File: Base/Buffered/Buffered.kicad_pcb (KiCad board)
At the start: 2 copper layers, 30 x 84 mm, 19 parts, among them J1 Conn_01x04_Pin, J2 Conn_01x04_Pin, J3 AudioJack2_Ground, J4 AudioJack2_Ground, J5 Barrel_Jack_Switch, Q1 40V, Q2 DMC3071LVT

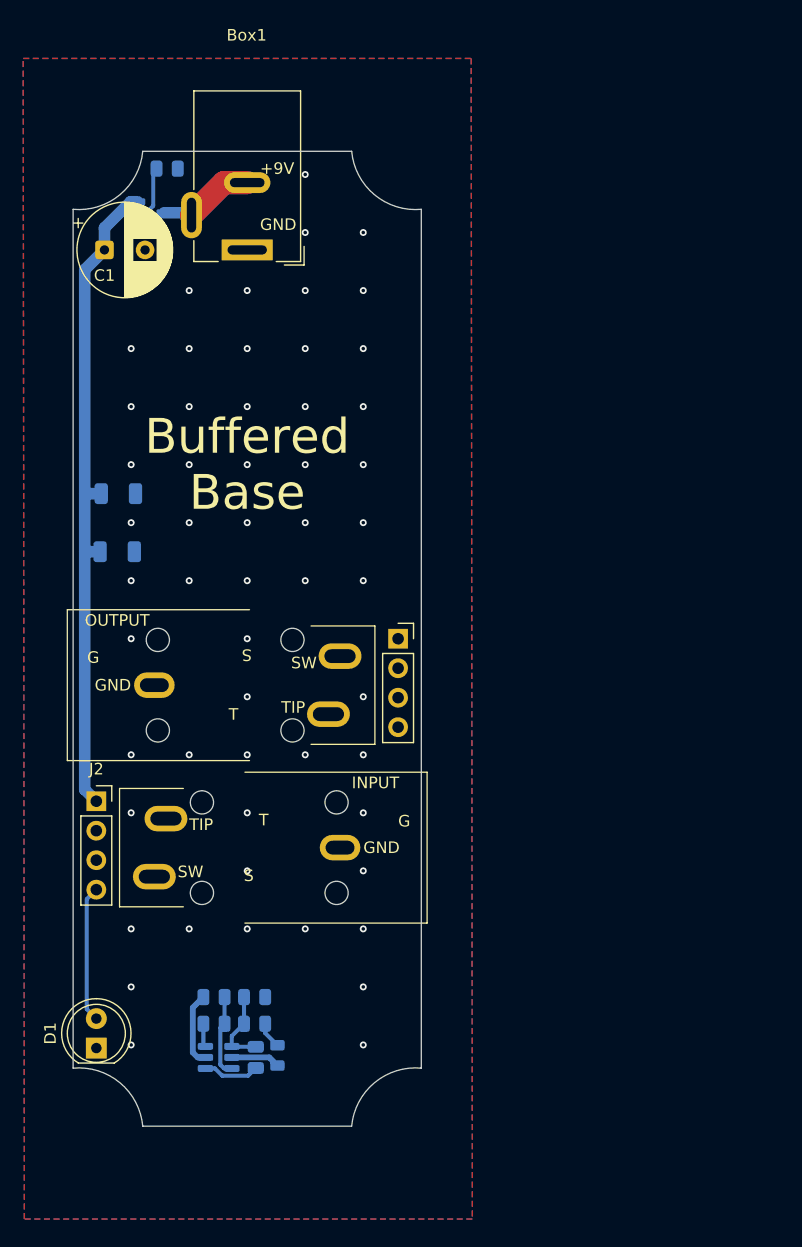
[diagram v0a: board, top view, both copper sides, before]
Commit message: Wire the soft-switch up to actually switch signal and LED
Surprisingly, this actually seems to work fine.  In simulation only, of
course.

And not surprisingly, according to the same simulation, it has an
impressively horrible pop at switching time.  This very much reminds me
of the broken "Tremolo doubling as a metronome" thing, which was due to
the exact same thing: very harsh and sudden driving of the JFET gate.

It's made worse by the MOSFET switching having the same thing.  Big
voltage spike when turning off, presumably due to capacitive parasitics
or whatever.

Possibly helped by adding a resistor at the gate or something, but
unlike the tremolo, the switching event is rare.  So right now I simply
don't care.  I'm just _simulating_ switching things at a 5Hz rate, so it
shows up like a sore thumb.

I haven't done layout, and I haven't added a real switch yet, so this is
all just simulation.

Signed-off-by: Linus Torvalds <torvalds@linux-foundation.org>
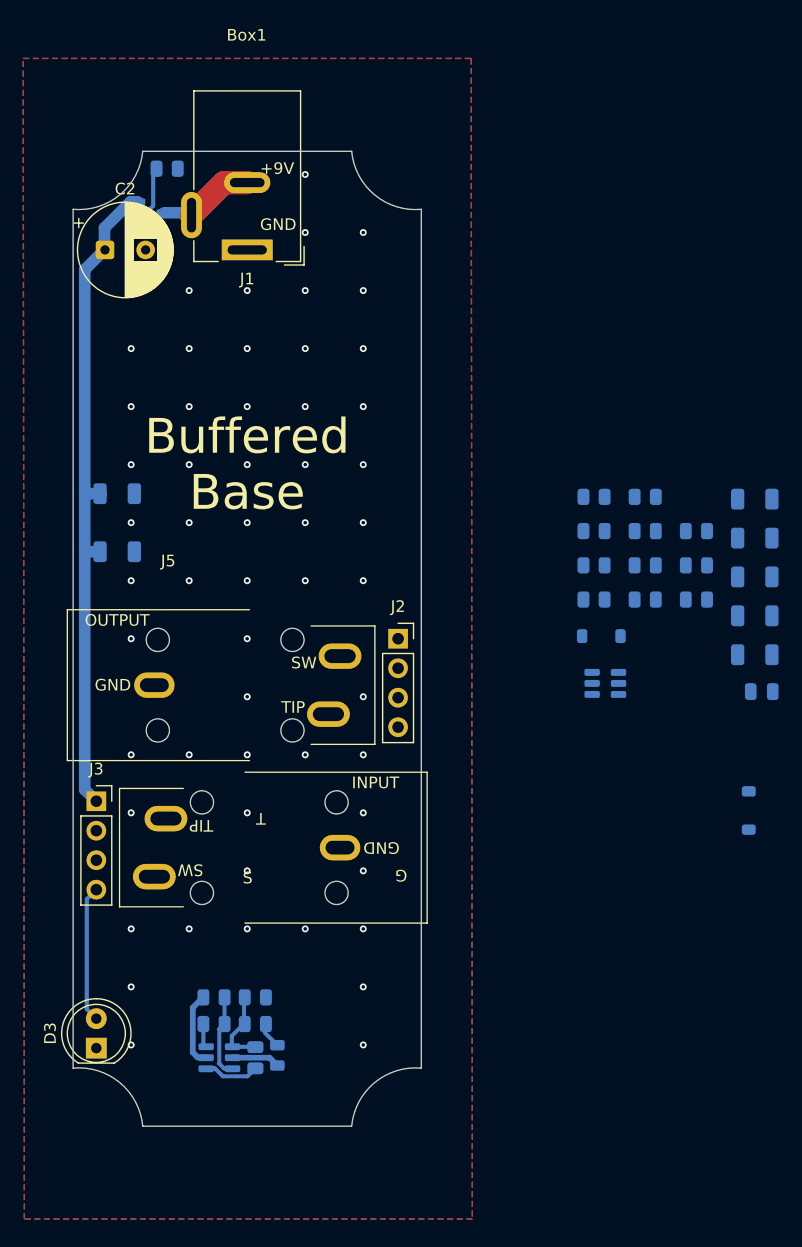
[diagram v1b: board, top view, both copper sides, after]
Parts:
- removed R1: 100k, Resistor_SMD:R_0805_2012Metric
- added C10: 1uF, Capacitor_SMD:C_1206_3216Metric, B.Cu at (143.7, 101.4)
- added C5: 1uF, Capacitor_SMD:C_1206_3216Metric, B.Cu at (143.7, 88.0)
- added C6: 1uF, Capacitor_SMD:C_1206_3216Metric, B.Cu at (143.7, 91.3)
- added C7: 0.47uF, Capacitor_SMD:C_1206_3216Metric, B.Cu at (143.7, 94.7)
- added C8: 220pF, Capacitor_SMD:C_0805_2012Metric, B.Cu at (144.3, 104.6)
- added C9: 1uF, Capacitor_SMD:C_1206_3216Metric, B.Cu at (143.7, 98.0)
- added D2: BAT41Z, Diode_SMD:D_SOD-123, B.Cu at (130.5, 99.8)
- added D3: LED, LED_THT:LED_D5.0mm, F.Cu at (87.0, 135.3)
- added Q3: LS844, Package_TO_SOT_SMD:SOT-23-6, B.Cu at (130.9, 103.8)
- added R10: 1MEG, Resistor_SMD:R_0805_2012Metric, B.Cu at (138.7, 96.6)
- added R11: 1MEG, Resistor_SMD:R_0805_2012Metric, B.Cu at (134.3, 87.8)
- added R12: 1k, Resistor_SMD:R_0805_2012Metric, B.Cu at (134.3, 90.7)
- added R13: 1MEG, Resistor_SMD:R_0805_2012Metric, B.Cu at (134.3, 93.7)
- added R14: 22k, Resistor_SMD:R_0805_2012Metric, B.Cu at (134.3, 96.6)
- added R15: 22k, Resistor_SMD:R_0805_2012Metric, B.Cu at (129.9, 87.8)
- added R16: 22k, Resistor_SMD:R_0805_2012Metric, B.Cu at (129.9, 90.7)
- added R17: 22k, Resistor_SMD:R_0805_2012Metric, B.Cu at (129.9, 93.7)
- added R18: 2k2, Resistor_SMD:R_0805_2012Metric, B.Cu at (129.9, 96.6)
- added R7: 22k, Resistor_SMD:R_0805_2012Metric, B.Cu at (100.7, 130.9)
- added R8: 1MEG, Resistor_SMD:R_0805_2012Metric, B.Cu at (138.7, 90.7)
- added R9: 1MEG, Resistor_SMD:R_0805_2012Metric, B.Cu at (138.7, 93.7)
- C1: value 100uF -> 0.1uF; footprint Capacitor_THT:CP_Radial_D8.0mm_P3.50mm -> Mylib:C_0704_1810Metric; moved to B.Cu
- C2: value 10uF -> 100uF; footprint Capacitor_SMD:C_1206_3216Metric -> Capacitor_THT:CP_Radial_D8.0mm_P3.50mm; moved to F.Cu
- C3: value 1uF -> 10uF
- C4: value 0.1uF -> 1uF; footprint Mylib:C_0704_1810Metric -> Capacitor_SMD:C_1206_3216Metric
- D1: value LED -> BAT41Z; footprint LED_THT:LED_D5.0mm -> Diode_SMD:D_SOD-123; moved to B.Cu
- J1: value Conn_01x04_Pin -> Barrel_Jack_Switch; footprint Connector_PinSocket_2.54mm:PinSocket_1x04_P2.54mm_Vertical -> Connector_BarrelJack:BarrelJack_Wuerth_6941xx301002
- J3: value AudioJack2_Ground -> Conn_01x04_Pin; footprint Mylib:CK-6.35 -> Connector_PinSocket_2.54mm:PinSocket_1x04_P2.54mm_Vertical
- J5: value Barrel_Jack_Switch -> AudioJack2_Ground; footprint Connector_BarrelJack:BarrelJack_Wuerth_6941xx301002 -> Mylib:CK-6.35
- Q1: value 40V -> DMC3071LVT; footprint Package_TO_SOT_SMD:SOT-23-3 -> Package_TO_SOT_SMD:TSOT-23-6
- Q2: value DMC3071LVT -> 40V; footprint Package_TO_SOT_SMD:TSOT-23-6 -> Package_TO_SOT_SMD:SOT-23-3
- R4: value 22k -> 100k
- R5: value 220k -> 22k
- R6: value 22k -> 220k
- moved Q1 73.0 mm to (97.6, 136.1)
- moved Q2 73.0 mm to (91.7, 63.3)
- moved R4 71.8 mm to (93.1, 59.5), turned to 0 degrees
- moved C1 71.0 mm to (102.6, 135.9), turned to -90 degrees
- moved D1 59.8 mm to (143.2, 114.8)
- moved C4 50.3 mm to (88.8, 87.5), turned to 0 degrees
- moved J5 38.3 mm to (92.0, 104.0), turned to 0 degrees
- moved J1 35.9 mm to (100.0, 66.5), turned to 180 degrees
- moved J2 29.5 mm to (113.0, 100.0)
- moved J3 21.4 mm to (87.0, 114.0), turned to 0 degrees
- moved J4 21.3 mm to (108.0, 118.0), turned to 180 degrees
- moved C2 21.0 mm to (87.7, 66.5)
- moved R5 2.93 mm to (100.7, 136.1), turned to -90 degrees
- moved R6 2.88 mm to (100.7, 133.2), turned to 180 degrees
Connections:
- C1 pad 1: VIN -> SW2
- C4 pad 1: SW2 -> VIN
- D1 pad 1: GND -> Net-(D1-K)
- D1 pad 2: LED -> GATE^{OFF}
- J1 pad 1: IN^{EFF} -> GND
- J1 pad 2: GND -> PWRIN
- J1 pad 3: GND -> PWRIN
- J2 pad 1: VIN -> IN^{EFF}
- J2 pad 4: LED -> OUT^{EFF}
- J4 pad S: unconnected-(J4-PadS) -> GND
- J4 pad T: OUT^{CONN} -> IN^{CONN}
- Q1 pad 1: Net-(Q1-G) -> Net-(Q1A-G)
- Q1 pad 3: PWRIN -> SW1
- Q2 pad 1: Net-(Q2A-G) -> Net-(Q2-G)
- Q2 pad 3: SW1 -> PWRIN
- R4 pad 1: GND -> Net-(Q2-G)
- R4 pad 2: ON_HIGH -> GND
- R5 pad 1: SW2 -> ON_HIGH
- R5 pad 2: ON_HIGH -> Net-(Q1A-G)
- R6 pad 1: ON_HIGH -> SW2
- R6 pad 2: Net-(Q2A-G) -> ON_HIGH
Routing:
- net Net-(Q2-G): track 0.00 -> 5.42 mm
- net Net-(Q1-G): track 5.42 -> 0.00 mm
- net Net-(Q1A-G): track 0.00 -> 4.91 mm
- net Net-(Q2A-G): track 4.87 -> 0.00 mm

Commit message: Split the buffered base over multiple schematic pages, do PCB layout
So this thing is still mis-named, in that it doesn't actually buffer the
signal at all, it only does the transistor soft-switching.  But I _will_
add buffering at some point, it's just not the interesting part of this
all, since I've done that part before.

But because I wrote explanations for the push-on / push-off circuit, and
because I split things up into small parts, the schematic was getting
pretty crowded.  So I decided to split up the actually interesting part
of the schematic - the switching side - onto a schematic page of its
own.

And while doing that, I moved the simulation infrastructure to its own
page too.

That leaves the toplevel page pretty empty with mainly just the
connectors and the basic signal and power filtering, but that's where
the buffers will go eventually.

And because it simulates fine, I want to actually see if it works in
reality.  So this also does the PCB layout.  There's tons of room left
for any future buffering circuit, whether I then do it with discrete
JFETs or decide that op-amps are the sane thing here.

I used a random regular tactile switch - which I don't actually have in
my parts library.  I'll just wire up two wires and test it that way (and
I do have some momentary SPDT stomp switches around that I can attach to
the wires).

But longer-term, one of the points of this kind of electronic switching
is that you can do it multiple ways, and aren't limited to a physical
switch - or indeed just a single one.  So maybe I'll do some remote
switching thing, or play around with using a hall effect sensor and a
magnet, or whatever.

There are always new things to learn about...  But let's make sure the
basics of this thing actually works first.

Signed-off-by: Linus Torvalds <torvalds@linux-foundation.org>
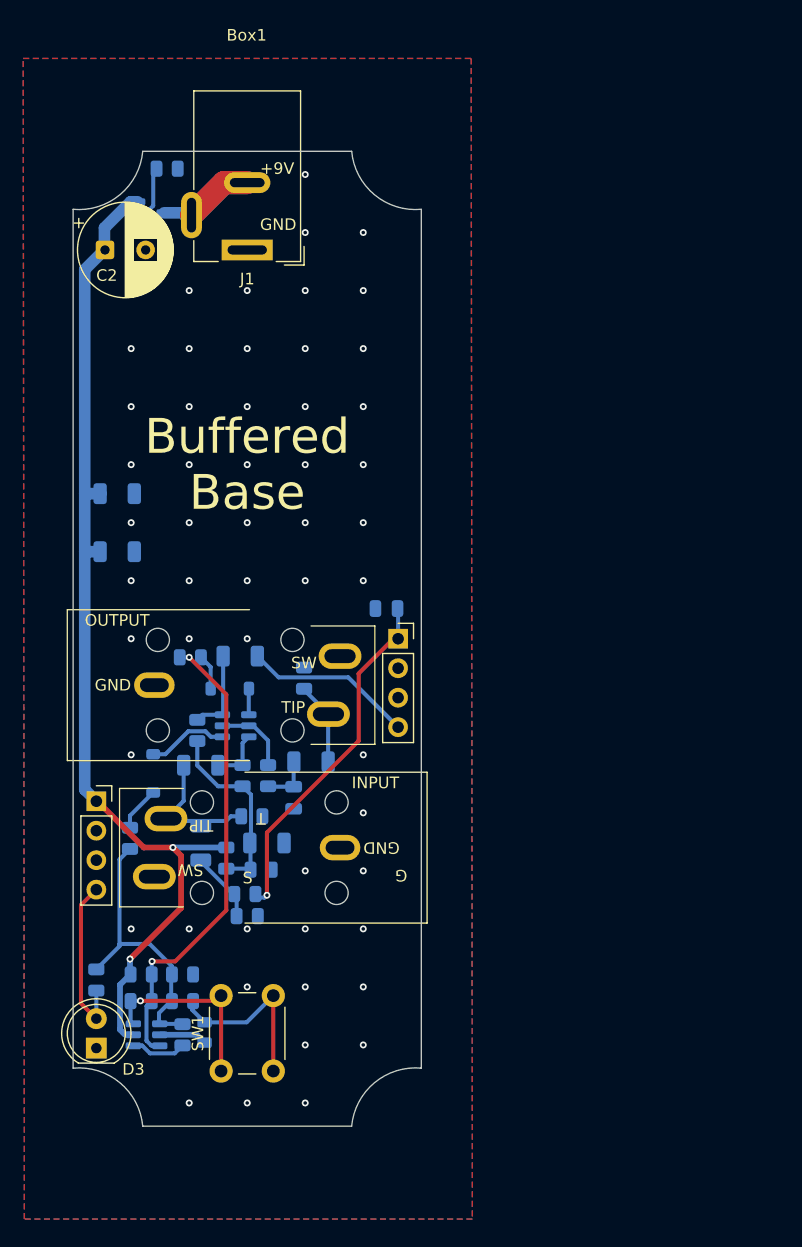
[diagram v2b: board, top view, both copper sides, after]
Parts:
- added C11: 150pF, Capacitor_SMD:C_0805_2012Metric, B.Cu at (104.0, 113.7)
- added R23: 1k, Resistor_SMD:R_0805_2012Metric, B.Cu at (101.8, 111.8)
- added SW1: SW_Push, Button_Switch_THT:SW_PUSH_6mm, F.Cu at (97.8, 137.2)
- C8: value 220pF -> 150pF
- R15: value 22k -> 47k
- moved R18 54.0 mm to (87.0, 129.4), turned to 90 degrees
- moved C7 53.0 mm to (96.0, 117.6), turned to -90 degrees
- moved C6 51.6 mm to (96.0, 110.9), turned to 0 degrees
- moved R11 49.8 mm to (100.0, 123.9), turned to 0 degrees
- moved R12 46.6 mm to (99.8, 122.0), turned to 0 degrees
- moved R17 46.4 mm to (89.9, 117.2), turned to -90 degrees
- moved C5 46.4 mm to (99.4, 101.5)
- moved R8 46.3 mm to (95.7, 107.9), turned to 90 degrees
- moved D1 45.9 mm to (98.5, 104.3), turned to 0 degrees
- moved C10 45.1 mm to (101.7, 117.6), turned to 0 degrees
- moved R9 43.1 mm to (99.6, 111.8), turned to -90 degrees
- moved R15 43.1 mm to (101.2, 119.9)
- moved R10 42.6 mm to (100.4, 115.3), turned to 0 degrees
- moved R14 42.4 mm to (98.2, 118.9), turned to 90 degrees
- moved D2 40.4 mm to (91.9, 111.6), turned to 90 degrees
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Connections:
- C6 pad 1: IN^{EFF} -> IN^{CONN}
- C9 pad 1: Net-(Q3A-D) -> Net-(C11-Pad1)
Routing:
- net ON_LOW: track 7.16 -> 40.5 mm, vias 0 -> 2
- net IN^{EFF}: track 0.00 -> 30.9 mm, vias 0 -> 1
- net VIN: track 63.5 -> 89.4 mm, vias 0 -> 2
- net ON_HIGH: track 6.76 -> 24.4 mm
- net MIDBIAS: track 0.00 -> 16.4 mm
- net OUT^{EFF}: track 0.00 -> 14.7 mm
- net SW1: track 2.00 -> 16.5 mm, vias 0 -> 1
- net SW2: track 2.28 -> 15.7 mm
- net IN^{CONN}: track 0.00 -> 12.0 mm
- net Net-(Q3A-S): track 0.00 -> 7.42 mm
- net OUT^{CONN}: track 0.00 -> 7.17 mm
- net GATE^{ON}: track 0.00 -> 6.98 mm
- net Net-(Q3A-D): track 0.00 -> 6.58 mm
- net Net-(C7-Pad2): track 0.00 -> 6.16 mm
- net Net-(Q3B-S): track 0.00 -> 4.79 mm
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
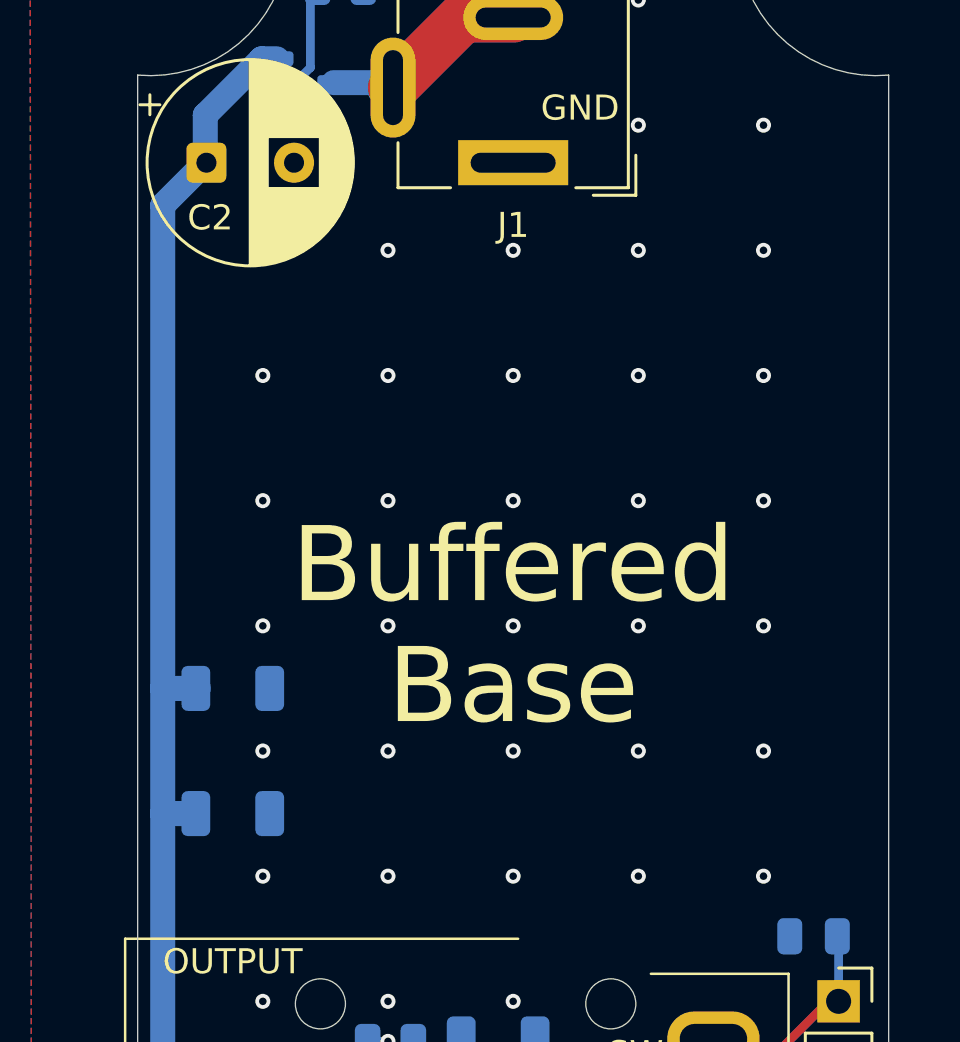
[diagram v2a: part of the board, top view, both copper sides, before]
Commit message: Add negative power rail to the buffered base design
The negative voltage isn't actually _used_ anywhere yet, but this is
prep-work for making that buffered base board do the long promised
buffering, as I'm currently leaning towards opamps.

The LT3462A is very easy to use, but in a probably completely misguided
attempt at keeping any stray ground return currents on the power supply
side, I added a ground plane keepout.  No isolation, but an attempt to
at least make the easy path for any return currents to stay in that
"power supply area" and hopefully not show up around the analog parts.

Somebody who knows what they are about would probably tell me I'm just
making things worse.  But I'm a sw engineer, so pretty much by
definition I don't know anybody who knows what they are doing.

Signed-off-by: Linus Torvalds <torvalds@linux-foundation.org>
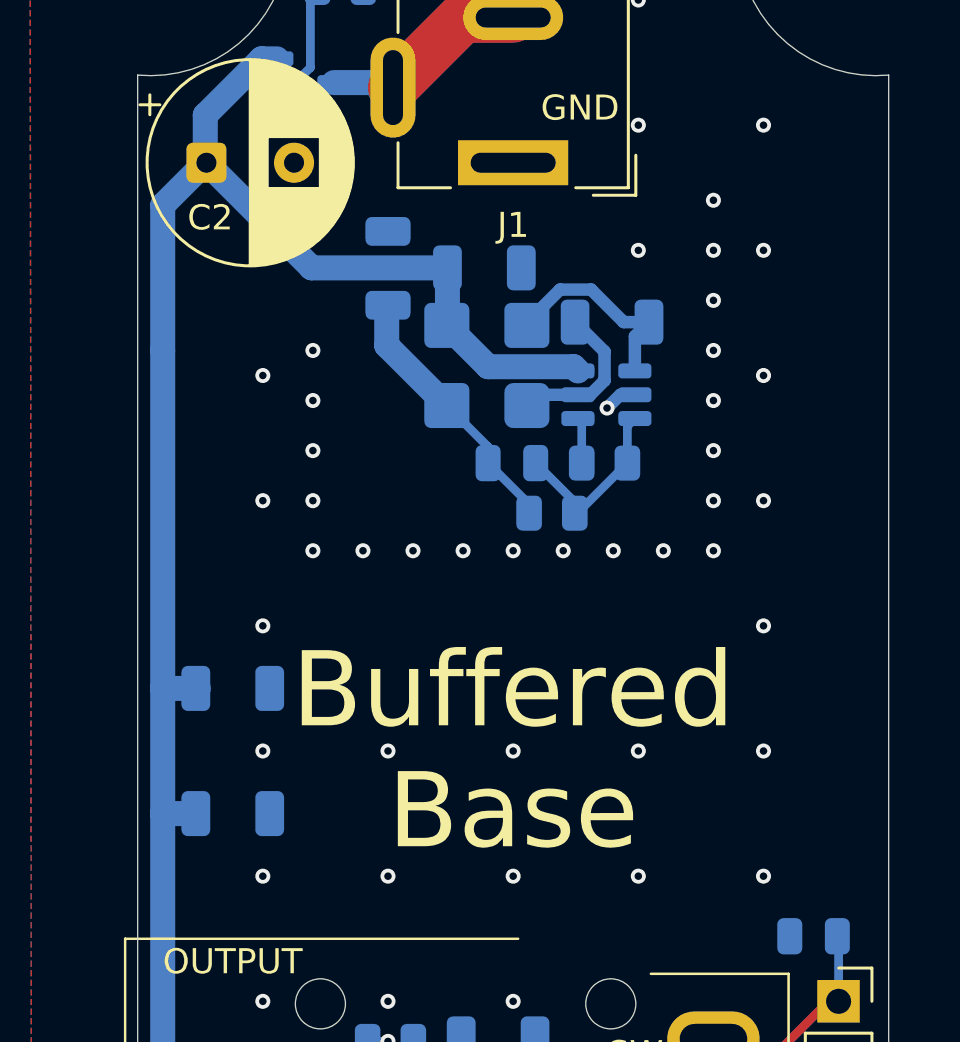
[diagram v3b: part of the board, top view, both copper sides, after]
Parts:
- added C12: 1uF, Capacitor_SMD:C_1206_3216Metric, B.Cu at (104.0, 72.9)
- added C13: 15pF, Capacitor_SMD:C_0805_2012Metric, B.Cu at (100.0, 78.5)
- added C14: 10uF, Capacitor_SMD:C_1206_3216Metric, B.Cu at (98.8, 70.7)
- added C15: 10uF, Capacitor_SMD:C_1206_3216Metric, B.Cu at (95.0, 70.7)
- added L1: 10uH, Mylib:LPD5030, B.Cu at (99.0, 74.6)
- added R24: 267k, Resistor_SMD:R_0805_2012Metric, B.Cu at (101.5, 80.5)
- added R25: 37.5k, Resistor_SMD:R_0805_2012Metric, B.Cu at (103.7, 78.5)
- added U1: LT3462A, Package_TO_SOT_SMD:TSOT-23-6, B.Cu at (103.7, 75.8)
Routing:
- net VIN: track 89.4 -> 109.1 mm
- net -V: track 0.00 -> 10.7 mm
- net Net-(U1-SW): track 0.00 -> 8.25 mm
- net Net-(U1-FB): track 0.00 -> 7.48 mm
- net Net-(U1-D): track 0.00 -> 6.33 mm
- net Net-(U1-SDREF): track 0.00 -> 1.84 mm
- net GND: track 4.14 -> 5.47 mm, vias 54 -> 63
